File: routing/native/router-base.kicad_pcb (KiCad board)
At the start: 4 copper layers, 46 x 46 mm, 71 parts, among them J1 J1, J2 J2, J3 J3, J4 J4, J5 J5, M1 M1, Q1 Q1, Q2 Q2, SW1 SW1, SW2 SW2, U1 NRF52810-QFAA-R, U2 BMA456, U3 HUSB238_002DD, U4 PCF8563TS/5,118, U5 BQ25180YBGR, U6 TPS63802DLAR, Y1 Y1, Y2 Y2, Y3 Y3

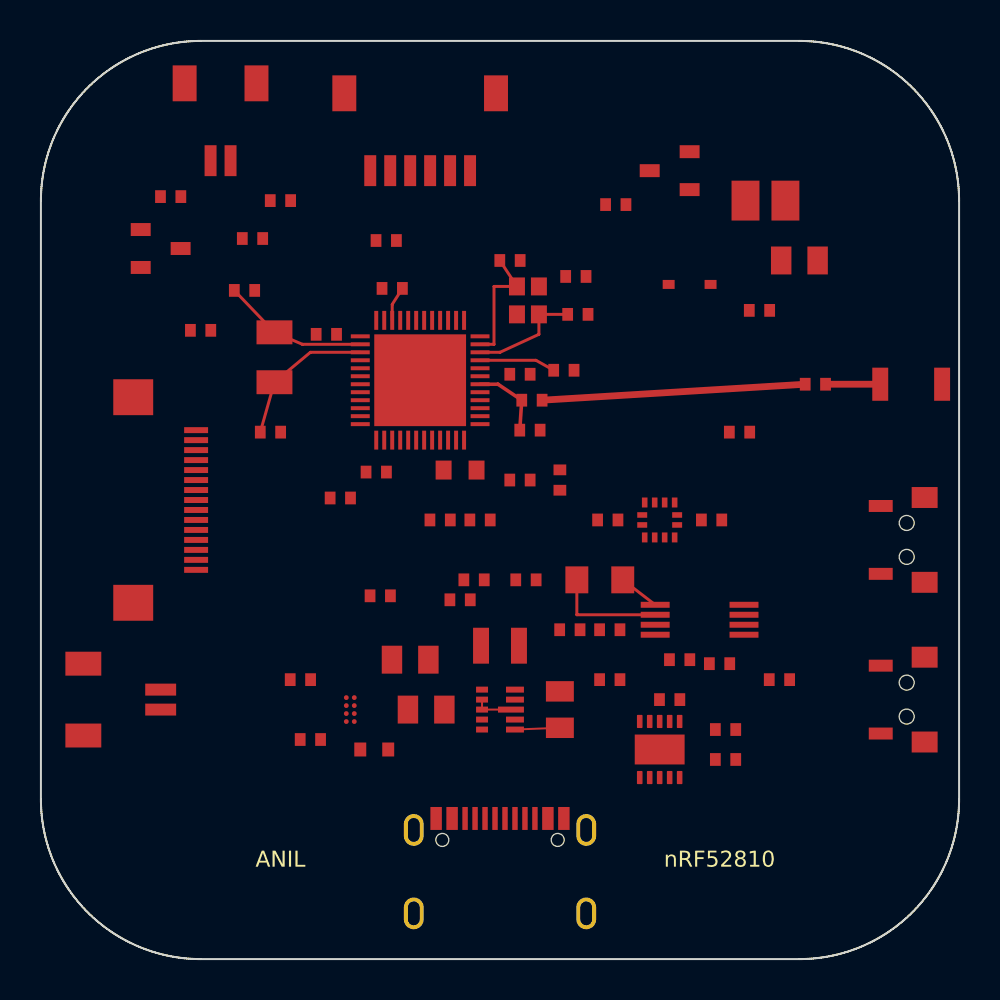
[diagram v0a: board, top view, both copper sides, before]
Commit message: Move charging port opposite centred buttons and reroute the assembly
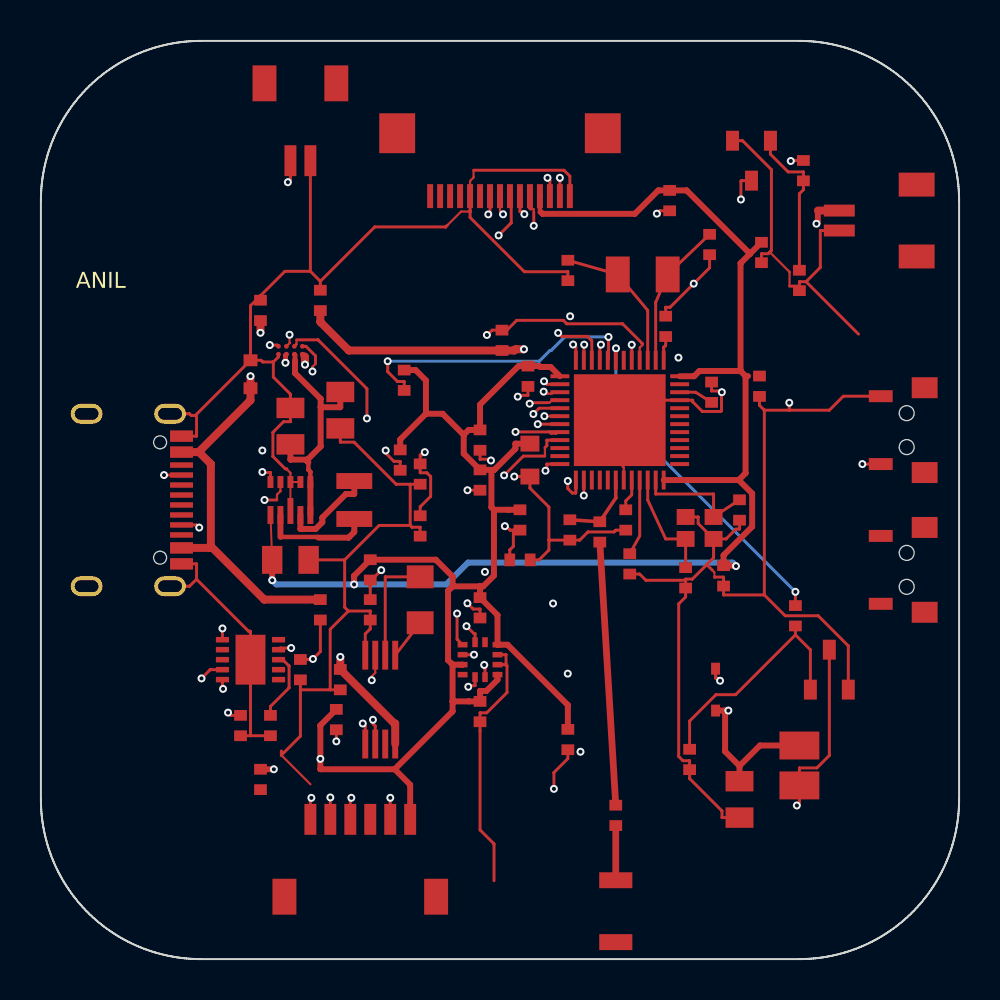
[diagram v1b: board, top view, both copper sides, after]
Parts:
- moved J3 36.6 mm to (93.0, 118.0)
- moved J2 33.4 mm to (119.0, 86.0)
- moved R15 31.7 mm to (115.2, 83.5)
- moved J5 30.4 mm to (90.0, 81.0)
- moved ANT1 30.3 mm to (105.8, 120.6)
- moved Q1 29.9 mm to (112.6, 83.0)
- moved M1 28.4 mm to (115.0, 113.3)
- moved C23 27.2 mm to (112.0, 115.0)
- moved R20 26.5 mm to (88.0, 114.0)
- moved R16 26.3 mm to (115.0, 89.0)
- moved Q2 26.2 mm to (116.5, 108.5)
- moved J1 26.1 mm to (81.6, 100.0)
- moved C15 25.5 mm to (113.1, 87.6)
- moved R14 24.4 mm to (108.5, 85.0)
- moved R2 24.4 mm to (87.0, 111.3)
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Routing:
- net GND: track 1.95 -> 284.2 mm, vias 0 -> 7
- net V3V0: track 2.25 -> 153.4 mm, vias 0 -> 6
- net BAT: track 0.00 -> 64.5 mm, vias 0 -> 4
- net I2C_SDA: track 0.00 -> 50.4 mm, vias 0 -> 5
- net BUTTON1: track 0.00 -> 41.1 mm, vias 0 -> 3
- net I2C_SCL: track 0.00 -> 38.1 mm, vias 0 -> 5
- net SWCLK: track 0.00 -> 25.7 mm, vias 0 -> 3
- net SWDIO: track 0.00 -> 25.6 mm, vias 0 -> 3
- net NRST: track 0.00 -> 25.4 mm, vias 0 -> 3
- net USB5V: track 0.00 -> 25.3 mm, vias 0 -> 3
- net DEBUG_GPIO: track 0.00 -> 25.2 mm, vias 0 -> 2
- net RTC_INT: track 0.00 -> 23.6 mm, vias 0 -> 3
- net LCD_BL: track 0.00 -> 21.2 mm, vias 0 -> 3
- net BAT_ADC: track 0.00 -> 20.6 mm, vias 0 -> 2
- net CHG_INT: track 0.00 -> 20.4 mm, vias 0 -> 3
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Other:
- board text removed: "nRF52810"
